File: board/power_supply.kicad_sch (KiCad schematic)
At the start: 39 parts, among them J1 USB, Q1 AP2302B, Q2 AP2302B, Q3 AP2302B, U1 ADP1613, U2 TP4054, U3 DW01A-G

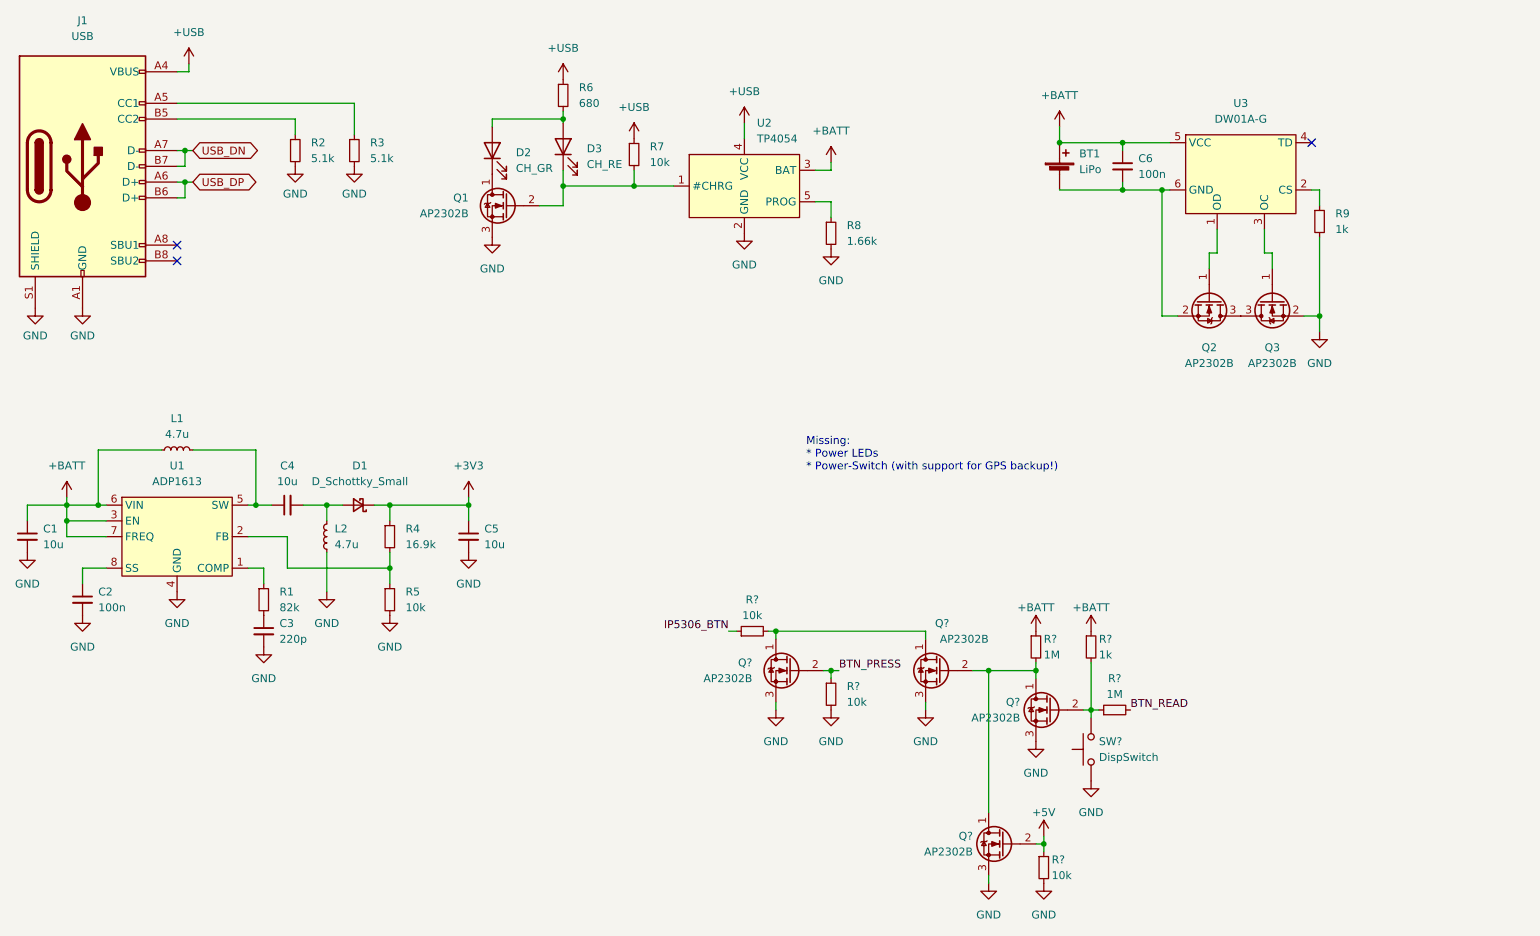
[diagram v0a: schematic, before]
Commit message: New power management IC, some cleanup
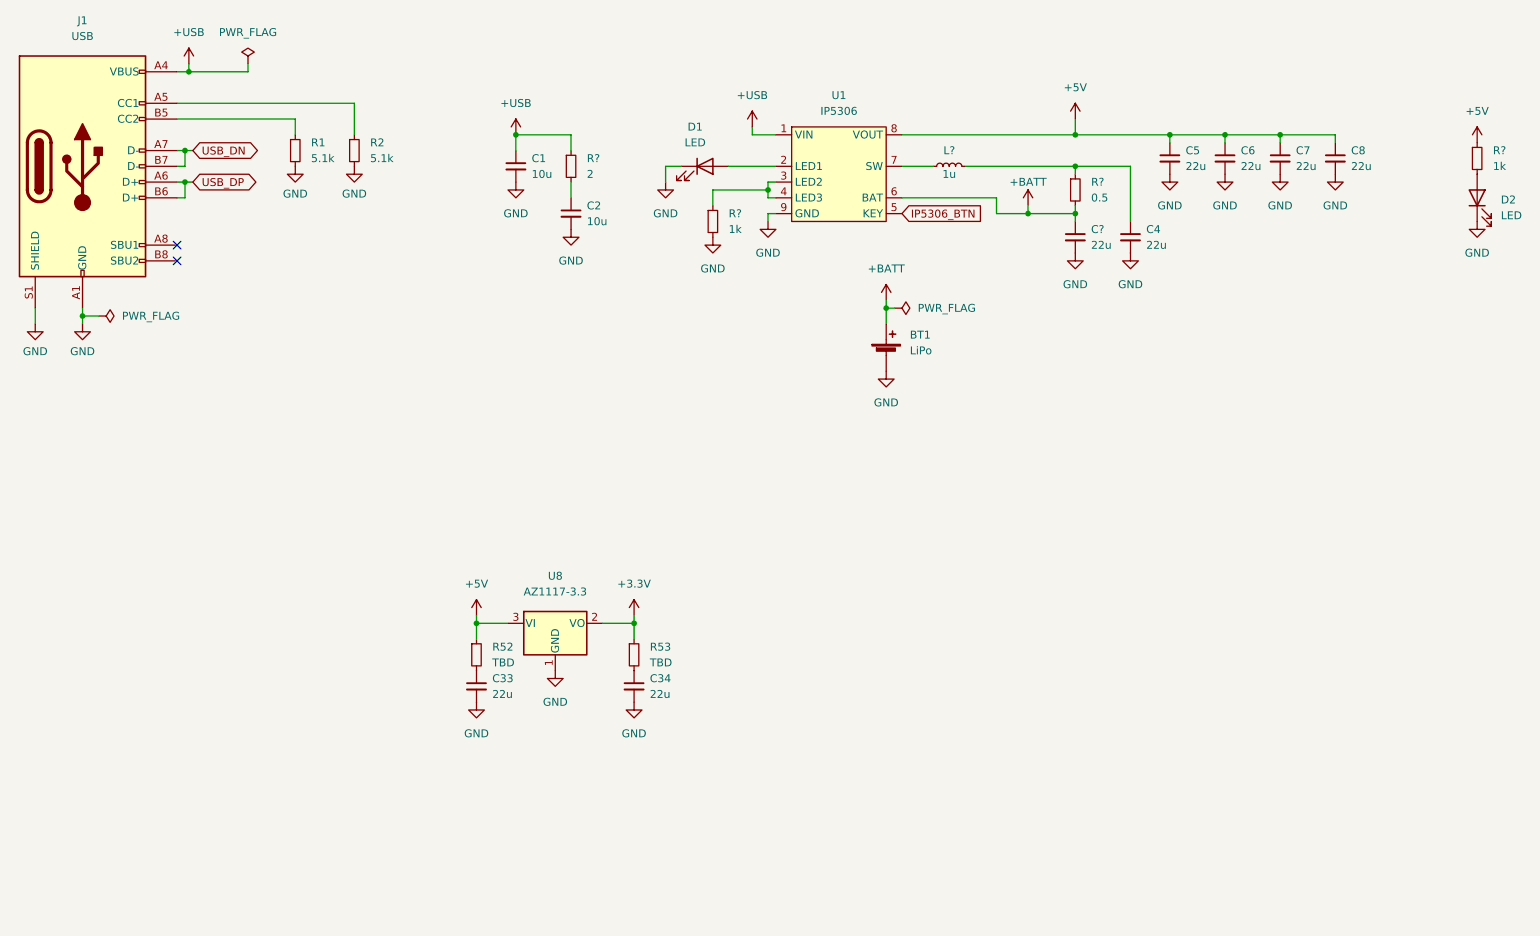
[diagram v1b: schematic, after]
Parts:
- removed C3: 220p, symbol Device:C_Small
- removed D1: D_Schottky_Small, symbol Device:D_Schottky_Small
- removed D3: CH_RE, symbol Device:LED
- removed L1, L2: 4.7u, symbol Device:L_Small
- removed Q1, Q? (x4): AP2302B, symbol Device:Q_NMOS_DGS
- removed Q2, Q3: AP2302B, symbol Device:Q_NMOS_GSD
- removed R1: 82k, symbol Device:R_Small
- removed R4: 16.9k, symbol Device:R_Small
- removed R5, R7, R? (x3): 10k, symbol Device:R_Small
- removed R6: 680, symbol Device:R_Small
- removed R8: 1.66k, symbol Device:R_Small
- removed R9, R?: 1k, symbol Device:R_Small
- removed R? (x2): 1M, symbol Device:R_Small
- removed SW?: DispSwitch, symbol Switch:SW_MEC_5G
- removed U1: ADP1613, symbol OBSPro:ADP1613
- removed U2: TP4054, symbol OBSPro:TP4054
- removed U3: DW01A-G, symbol OBSPro:DW01x
- added C33, C34, C7, C8, C?: 22u, Capacitor_SMD:C_1206_3216Metric, symbol Device:C_Small
- added D1: LED, LED_SMD:LED_0603_1608Metric, symbol Device:LED
- added L?: 1u, Inductor_SMD:L_Vishay_IFSC-1515AH_4x4x1.8mm, symbol Device:L_Small
- added R52, R53: TBD, symbol Device:R_Small
- added R?: 2, Resistor_SMD:R_0603_1608Metric, symbol Device:R_Small
- added R?: 0.5, Resistor_SMD:R_0603_1608Metric, symbol Device:R_Small
- added R? (x2): 1k, Resistor_SMD:R_0603_1608Metric, symbol Device:R_Small
- added U1: IP5306, symbol OBSPro:IP5306
- added U8: AZ1117-3.3, symbol Regulator_Linear:AZ1117-3.3
- BT1: Comment You need 2 per PCB! -> (none); JLC_BasicPart no -> (none); JLC_PN C2979182 -> (none); JLC_Price1 0.591 -> (none); JLC_Price10 0.591 -> (none); JLC_Price100 0.4208 -> (none); JLC_Price1000 0.3288 -> (none); MPN MY-18650-02 -> (none); Manufacturer MYOUNG -> (none); PCBA no -> (none)
- C1: footprint (none) -> Capacitor_SMD:C_0603_1608Metric
- C2: value 100n -> 10u; footprint (none) -> Capacitor_SMD:C_0603_1608Metric; JLC_PN C14663 -> C19702; JLC_Price1 0.042 -> 0.062; JLC_Price10 0.0042 -> 0.0062; JLC_Price100 0.0021 -> 0.0031; JLC_Price1000 0.0014 -> 0.0029; MPN CC0603KRX7R9BB104 -> CL10A106KP8NNNC; Manufacturer YAGEO -> Samsung Electro-Mechanics
- C4, C5: value 10u -> 22u; footprint (none) -> Capacitor_SMD:C_1206_3216Metric; JLC_PN C19702 -> C5672; JLC_Price1 0.062 -> (none); JLC_Price10 0.0062 -> (none); JLC_Price100 0.0031 -> (none); JLC_Price1000 0.0029 -> (none); MPN CL10A106KP8NNNC -> CL31A226KPHNNNE
- C6: value 100n -> 22u; footprint (none) -> Capacitor_SMD:C_1206_3216Metric; JLC_PN C14663 -> C5672; JLC_Price1 0.042 -> (none); JLC_Price10 0.0042 -> (none); JLC_Price100 0.0021 -> (none); JLC_Price1000 0.0014 -> (none); MPN CC0603KRX7R9BB104 -> CL31A226KPHNNNE; Manufacturer YAGEO -> Samsung Electro-Mechanics
- D2: value CH_GR -> LED; footprint (none) -> LED_SMD:LED_0603_1608Metric; JLC_PN C2297 -> C2286; JLC_Price1 0.274 -> 0.106; JLC_Price10 0.0274 -> 0.0106; JLC_Price100 0.0137 -> 0.0053; JLC_Price1000 0.0096 -> 0.0036; MPN C2297 -> KT-0603R
- renumbered R2 to R1, R3 to R2
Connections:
- net +3V3 is gone; now on net +5V: C5.1
- net +5V: now also C6.1, C7.1, C8.1, R52.1, R?.1, U1.8 (VOUT), U8.3 (VI)
- net +BATT: now also C?.1, R?.2, U1.6 (BAT); no longer C1.1, C6.1
- net +USB: now also C1.1, R?.1, U1.1 (VIN)
- net GND: now also BT1.2 (-), C4.2, C6.2, D2.1 (K), C33.2, C34.2, C7.2, C8.2, C?.2, D1.1 (K), R?.2, U1.9 (GND), U8.1 (GND)
- net IP5306_BTN: now also U1.5 (KEY)
- net at D2.2 (A): now also R?.2
- net at C4.1: now also L?.2, R?.1
- net at C2.1: now also R?.2
- new net: C33.1, R52.2
- new net: C34.1, R53.2
- new net: L?.1, U1.7 (SW)
- new net: D1.2 (A), U1.2 (LED1)
- new net: R?.1, U1.3 (LED2), U1.4 (LED3)
- new net +3.3V: R53.1, U8.2 (VO)
- no-connect marks 3 -> 2
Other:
- note removed: "Missing: * Power LEDs * Power-Switch (with support for GPS backup!)"

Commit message: Add kibot:JLC:pricing from existing columns
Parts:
- C1, C2: kicost:JLC:pricing (none) -> 1: USD 0.062; 10: USD 0.0062; 100: USD 0.0031; 1000: USD0.0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
- D1, D2: kicost:JLC:pricing (none) -> 1: USD 0.106; 10: USD 0.0106; 100: USD 0.0053; 1000: USD0.0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
- J1: kicost:JLC:pricing (none) -> 1: USD 0.1675; 10: USD 0.1309; 100: USD 0.0972; 1000: USD0.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
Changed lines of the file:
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@@
+      (effects (font (size 1.27 1.27)) hide)
+    )
+    (property "kicost:JLC:pricing" "1: USD 0.062; 10: USD 0.0062; 100: USD 0.0031; 1000: USD0.0029" (id 13) (at 115.57 49.53 0)
       (effects (font (size 1.27 1.27)) hide)
     )
@@
     )
     (property "PCBA" "yes" (id 12) (at 106.68 41.91 0)
+      (effects (font (size 1.27 1.27)) hide)
+    )
+    (property "kicost:JLC:pricing" "1: USD 0.062; 10: USD 0.0062; 100: USD 0.0031; 1000: USD0.0029" (id 13) (at 106.68 41.91 0)
       (effects (font (size 1.27 1.27)) hide)
     )
@@
       (effects (font (size 1.27 1.27)) hide)
     )
+    (property "kicost:JLC:pricing" "1: USD 0.106; 10: USD 0.0106; 100: USD 0.0053; 1000: USD0.0036" (id 13) (at 137.16 41.91 0)
+      (effects (font (size 1.27 1.27)) hide)
+    )
     (pin "1")
     (pin "2")
@@
     )
     (property "PCBA" "yes" (id 12) (at 36.83 41.91 0)
+      (effects (font (size 1.27 1.27)) hide)
+    )
+    (property "kicost:JLC:pricing" "1: USD 0.1675; 10: USD 0.1309; 100: USD 0.0972; 1000: USD0.0902" (id 13) (at 36.83 41.91 0)
       (effects (font (size 1.27 1.27)) hide)
     )
@@
       (effects (font (size 1.27 1.27)) hide)
     )
+    (property "kicost:JLC:pricing" "1: USD 0.106; 10: USD 0.0106; 100: USD 0.0053; 1000: USD0.0036" (id 13) (at 261.62 46.99 0)
+      (effects (font (size 1.27 1.27)) hide)
+    )

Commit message: Add more footprints, prices and part numbers
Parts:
- C1, C2: kicost:JLC:pricing 1: USD 0.062; 10: USD 0.0062; 100: USD 0.0031; 1000: USD0.0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 -> 1: USD 0.062; 10: USD 0.0062; 100: USD 0.0031; 1000: USD 0.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
- C33, C34, C4, C5, C6, C7, C8, C?: kicost:JLC:pricing (none) -> 1: USD 0.0192; 150: USD 0.0186
- D1, D2: kicost:JLC:pricing 1: USD 0.106; 10: USD 0.0106; 100: USD 0.0053; 1000: USD0.0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 -> 1: USD 0.106; 10: USD 0.0106; 100: USD 0.0053; 1000: USD 0.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
- J1: kicost:JLC:pricing 1: USD 0.1675; 10: USD 0.1309; 100: USD 0.0972; 1000: USD0.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 -> 1: USD 0.1675; 10: USD 0.1309; 100: USD 0.0972; 1000: USD 0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
- L?: kicost:JLC:pricing (none) -> 1: USD 0.0815; 50: USD 0.0672; 150: USD 0.0600; 500: USD 0.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
- R1, R2: footprint (none) -> Resistor_SMD:R_0603_1608Metric; JLC_BasicPart (none) -> yes; JLC_PN (none) -> C23186; MPN (none) -> 0603WAF5101T5E; Manufacturer (none) -> UNI-ROYAL(Uniroyal Elec); kicost:JLC:pricing (none) -> 1: USD 0.0009; 200: USD 0.0007; 1000: USD 0.0006; 10000: US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
- R52, R53: PCBA (none) -> yes
- R?: kicost:JLC:pricing (none) -> 1: USD 0.0014; 200: USD 0.0011; 1000: USD 0.0009
- R?: kicost:JLC:pricing (none) -> 1: USD 0.0044; 200: USD 0.0037; 1000: USD 0.0033; 2000: USD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
- R? (x2): kicost:JLC:pricing (none) -> 1: USD 0.0005; 200: USD 0.0004
- U1: footprint (none) -> Package_SO:HSOP-8-1EP_3.9x4.9mm_P1.27mm_EP2.3x2.3mm; JLC_BasicPart (none) -> no; JLC_PN (none) -> C181692; MPN (none) -> IP5306; Manufacturer (none) -> INJOINIC; PCBA (none) -> yes; kicost:JLC:pricing (none) -> 1: USD 0.2895; 10: USD 0.2292; 30: USD 0.1998; 100: USD 0.1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
- U8: PCBA (none) -> yes; kicost:JLC:pricing (none) -> 1: USD 0.1347; 20: USD 0.1073; 60: USD 0.0956; 200: USD 0.0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
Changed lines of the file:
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@@
+      (effects (font (size 1.27 1.27)) hide)
+    )
+    (property "kicost:JLC:pricing" "1: USD 0.0192; 150: USD 0.0186" (id 9) (at 100.33 125.73 0)
       (effects (font (size 1.27 1.27)) hide)
     )
@@
       (effects (font (size 1.27 1.27)) hide)
     )
+    (property "kicost:JLC:pricing" "1: USD 0.0192; 150: USD 0.0186" (id 9) (at 238.76 40.64 0)
+      (effects (font (size 1.27 1.27)) hide)
+    )
     (pin "1")
     (pin "2")
@@
     )
     (property "PCBA" "yes" (id 11) (at 196.85 53.34 0)
+      (effects (font (size 1.27 1.27)) hide)
+    )
+    (property "kicost:JLC:pricing" "1: USD 0.0192; 150: USD 0.0186" (id 12) (at 196.85 53.34 0)
       (effects (font (size 1.27 1.27)) hide)
     )
@@
       (effects (font (size 1.27 1.27)) hide)
     )
+    (property "kicost:JLC:pricing" "1: USD 0.0192; 150: USD 0.0186" (id 9) (at 125.73 125.73 0)
+      (effects (font (size 1.27 1.27)) hide)
+    )
     (pin "1")
     (pin "2")
@@
     )
     (property "MPN" "0603WAF200KT5E" (id 11) (at 115.57 41.91 0)
+      (effects (font (size 1.27 1.27)) hide)
+    )
+    (property "kicost:JLC:pricing" "1: USD 0.0014; 200: USD 0.0011; 1000: USD 0.0009" (id 12) (at 115.57 41.91 0)
       (effects (font (size 1.27 1.27)) hide)
     )
@@
       (effects (font (size 1.27 1.27)) hide)
     )
+    (property "kicost:JLC:pricing" "1: USD 0.0815; 50: USD 0.0672; 150: USD 0.0600; 500: USD 0.0546; 3000: USD 0.0504; 6000: USD 0.0483" (id 12) (at 176.53 41.91 0)
+      (effects (font (size 1.27 1.27)) hide)
+    )
     (pin "1")
     (pin "2")
@@
       (effects (font (size 1.27 1.27)) hide)
     )
+    (property "kicost:JLC:pricing" "1: USD 0.0044; 200: USD 0.0037; 1000: USD 0.0033; 2000: USD 0.0032; 10000: USD 0.0029; 20000: USD 0.0028" (id 12) (at 196.85 45.72 0)
+      (effects (font (size 1.27 1.27)) hide)
+    )
     (pin "1")
     (pin "2")
@@
       (effects (font (size 1.27 1.27)) hide)
     )
-    (property "kicost:JLC:pricing" "1: USD 0.062; 10: USD 0.0062; 100: USD 0.0031; 1000: USD0.0029" (id 13) (at 115.57 49.53 0)
+    (property "kicost:JLC:pricing" "1: USD 0.062; 10: USD 0.0062; 100: USD 0.0031; 1000: USD 0.0029" (id 13) (at 115.57 49.53 0)
       (effects (font (size 1.27 1.27)) hide)
     )
@@
     )
     (property "PCBA" "yes" (id 8) (at 205.74 53.34 0)
+      (effects (font (size 1.27 1.27)) hide)
+    )
+    (property "kicost:JLC:pricing" "1: USD 0.0192; 150: USD 0.0186" (id 9) (at 205.74 53.34 0)
       (effects (font (size 1.27 1.27)) hide)
     )
@@
       (effects (font (size 1.27 1.27)) hide)
     )
+    (property "kicost:JLC:pricing" "1: USD 0.0192; 150: USD 0.0186" (id 9) (at 229.87 40.64 0)
+      (effects (font (size 1.27 1.27)) hide)
+    )
     (pin "1")
     (pin "2")
@@
       (effects (font (size 1.27 1.27)) hide)
     )
-    (property "kicost:JLC:pricing" "1: USD 0.062; 10: USD 0.0062; 100: USD 0.0031; 1000: USD0.0029" (id 13) (at 106.68 41.91 0)
+    (property "kicost:JLC:pricing" "1: USD 0.062; 10: USD 0.0062; 100: USD 0.0031; 1000: USD 0.0029" (id 13) (at 106.68 41.91 0)
       (effects (font (size 1.27 1.27)) hide)
     )
@@
     (property "Reference" "U1" (id 0) (at 158.75 30.48 0))
     (property "Value" "IP5306" (id 1) (at 158.75 33.02 0))
-    (property "Footprint" "" (id 2) (at 158.75 44.45 0)
+    (property "Footprint" "Package_SO:HSOP-8-1EP_3.9x4.9mm_P1.27mm_EP2.3x2.3mm" (id 2) (at 158.75 44.45 0)
       (effects (font (size 1.27 1.27)) hide)
     )
     (property "Datasheet" "" (id 3) (at 158.75 44.45 0)
+      (effects (font (size 1.27 1.27)) hide)
+    )
+    (property "JLC_BasicPart" "no" (id 4) (at 158.75 41.91 0)
+      (effects (font (size 1.27 1.27)) hide)
+    )
+    (property "JLC_PN" "C181692" (id 5) (at 158.75 41.91 0)
+      (effects (font (size 1.27 1.27)) hide)
+    )
+    (property "MPN" "IP5306" (id 6) (at 158.75 41.91 0)
+      (effects (font (size 1.27 1.27)) hide)
+    )
+    (property "Manufacturer" "INJOINIC" (id 7) (at 158.75 41.91 0)
+      (effects (font (size 1.27 1.27)) hide)
+    )
+    (property "PCBA" "yes" (id 8) (at 158.75 41.91 0)
+      (effects (font (size 1.27 1.27)) hide)
+    )
+    (property "kicost:JLC:pricing" "1: USD 0.2895; 10: USD 0.2292; 30: USD 0.1998; 100: USD 0.1734; 500: USD 0.1662; 4000: USD 0.1592; 800: USD 0.1619; 1600: USD 0.1605" (id 9) (at 158.75 41.91 0)
       (effects (font (size 1.27 1.27)) hide)
     )
@@
       (effects (font (size 1.27 1.27)) hide)
     )
-    (property "kicost:JLC:pricing" "1: USD 0.106; 10: USD 0.0106; 100: USD 0.0053; 1000: USD0.0036" (id 13) (at 137.16 41.91 0)
+    (property "kicost:JLC:pricing" "1: USD 0.106; 10: USD 0.0106; 100: USD 0.0053; 1000: USD 0.0036" (id 13) (at 137.16 41.91 0)
       (effects (font (size 1.27 1.27)) hide)
     )
@@
       (effects (font (size 1.27 1.27)) hide)
     )
+    (property "PCBA" "yes" (id 4) (at 113.03 115.57 0)
+      (effects (font (size 1.27 1.27)) hide)
+    )
+    (property "kicost:JLC:pricing" "1: USD 0.1347; 20: USD 0.1073; 60: USD 0.0956; 200: USD 0.0810; 1000: USD 0.0744; 2000: USD 0.0705" (id 5) (at 113.03 115.57 0)
+      (effects (font (size 1.27 1.27)) hide)
+    )
     (pin "1")
     (pin "2")
@@
       (effects (font (size 1.27 1.27)) hide)
     )
-    (property "kicost:JLC:pricing" "1: USD 0.1675; 10: USD 0.1309; 100: USD 0.0972; 1000: USD0.0902" (id 13) (at 36.83 41.91 0)
+    (property "kicost:JLC:pricing" "1: USD 0.1675; 10: USD 0.1309; 100: USD 0.0972; 1000: USD 0.0902" (id 13) (at 36.83 41.91 0)
       (effects (font (size 1.27 1.27)) hide)
     )
@@
       (effects (font (size 1.27 1.27)) hide)
     )
+    (property "kicost:JLC:pricing" "1: USD 0.0005; 200: USD 0.0004" (id 12) (at 261.62 40.64 0)
+      (effects (font (size 1.27 1.27)) hide)
+    )
     (pin "1")
     (pin "2")
@@
       (effects (font (size 1.27 1.27)) hide)
     )
+    (property "PCBA" "yes" (id 4) (at 100.33 120.65 0)
+      (effects (font (size 1.27 1.27)) hide)
+    )
     (pin "1")
     (pin "2")
@@
       (effects (font (size 1.27 1.27)) (justify left))
     )
-    (property "Footprint" "" (id 2) (at 80.645 39.37 0)
+    (property "Footprint" "Resistor_SMD:R_0603_1608Metric" (id 2) (at 80.645 39.37 0)
       (effects (font (size 1.27 1.27)) hide)
     )
@@
     )
     (property "PCBA" "yes" (id 4) (at 80.645 39.37 0)
+      (effects (font (size 1.27 1.27)) hide)
+    )
+    (property "JLC_BasicPart" "yes" (id 5) (at 80.645 39.37 0)
+      (effects (font (size 1.27 1.27)) hide)
+    )
+    (property "JLC_PN" "C23186" (id 6) (at 80.645 39.37 0)
+      (effects (font (size 1.27 1.27)) hide)
+    )
+    (property "MPN" "0603WAF5101T5E" (id 7) (at 80.645 39.37 0)
+      (effects (font (size 1.27 1.27)) hide)
+    )
+    (property "Manufacturer" "UNI-ROYAL(Uniroyal Elec)" (id 8) (at 80.645 39.37 0)
+      (effects (font (size 1.27 1.27)) hide)
+    )
+    (property "kicost:JLC:pricing" "1: USD 0.0009; 200: USD 0.0007; 1000: USD 0.0006; 10000: USD 0.0005" (id 9) (at 80.645 39.37 0)
       (effects (font (size 1.27 1.27)) hide)
     )
@@
       (effects (font (size 1.27 1.27)) hide)
     )
+    (property "kicost:JLC:pricing" "1: USD 0.0192; 150: USD 0.0186" (id 9) (at 212.09 40.64 0)
+      (effects (font (size 1.27 1.27)) hide)
+    )
     (pin "1")
     (pin "2")
@@
       (effects (font (size 1.27 1.27)) hide)
     )
-    (property "kicost:JLC:pricing" "1: USD 0.106; 10: USD 0.0106; 100: USD 0.0053; 1000: USD0.0036" (id 13) (at 261.62 46.99 0)
+    (property "kicost:JLC:pricing" "1: USD 0.106; 10: USD 0.0106; 100: USD 0.0053; 1000: USD 0.0036" (id 13) (at 261.62 46.99 0)
       (effects (font (size 1.27 1.27)) hide)
     )
@@
       (effects (font (size 1.27 1.27)) (justify left))
     )
-    (property "Footprint" "" (id 2) (at 71.12 39.37 0)
+    (property "Footprint" "Resistor_SMD:R_0603_1608Metric" (id 2) (at 71.12 39.37 0)
       (effects (font (size 1.27 1.27)) hide)
     )
@@
     )
     (property "PCBA" "yes" (id 4) (at 71.12 39.37 0)
+      (effects (font (size 1.27 1.27)) hide)
+    )
+    (property "JLC_BasicPart" "yes" (id 5) (at 71.12 39.37 0)
+      (effects (font (size 1.27 1.27)) hide)
+    )
+    (property "JLC_PN" "C23186" (id 6) (at 71.12 39.37 0)
+      (effects (font (size 1.27 1.27)) hide)
+    )
+    (property "MPN" "0603WAF5101T5E" (id 7) (at 71.12 39.37 0)
+      (effects (font (size 1.27 1.27)) hide)
+    )
+    (property "Manufacturer" "UNI-ROYAL(Uniroyal Elec)" (id 8) (at 71.12 39.37 0)
+      (effects (font (size 1.27 1.27)) hide)
+    )
+    (property "kicost:JLC:pricing" "1: USD 0.0009; 200: USD 0.0007; 1000: USD 0.0006; 10000: USD 0.0005" (id 9) (at 71.12 39.37 0)
       (effects (font (size 1.27 1.27)) hide)
     )
@@
       (effects (font (size 1.27 1.27)) hide)
     )
+    (property "kicost:JLC:pricing" "1: USD 0.0005; 200: USD 0.0004" (id 12) (at 138.43 50.8 0)
+      (effects (font (size 1.27 1.27)) hide)
+    )
     (pin "1")
     (pin "2")
@@
       (effects (font (size 1.27 1.27)) hide)
     )
+    (property "kicost:JLC:pricing" "1: USD 0.0192; 150: USD 0.0186" (id 9) (at 220.98 40.64 0)
+      (effects (font (size 1.27 1.27)) hide)
+    )
     (pin "1")
     (pin "2")
@@
       (effects (font (size 1.27 1.27)) hide)
     )
+    (property "PCBA" "yes" (id 4) (at 125.73 120.65 0)
+      (effects (font (size 1.27 1.27)) hide)
+    )
